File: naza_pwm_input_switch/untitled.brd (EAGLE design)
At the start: 86.3 x 50.5 mm, 30 parts, among them T1 BC847, T10 BC847, T11 BC847, T12 BC847, T2 BC847, T3 BC847, T4 BC847, T5 BC847, T6 BC847, T7 BC847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

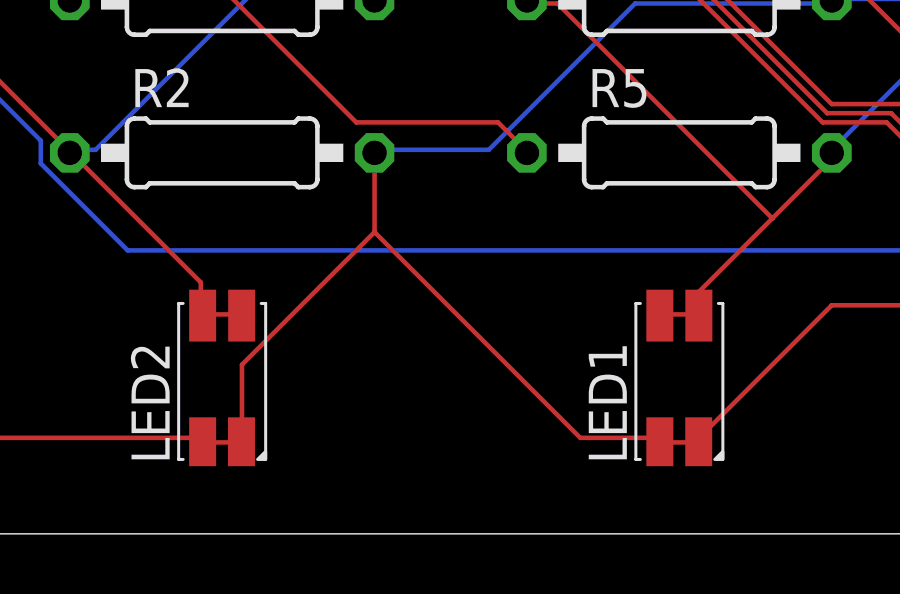
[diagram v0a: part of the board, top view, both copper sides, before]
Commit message: adjusting PCB-pwm-input-switch led voltage
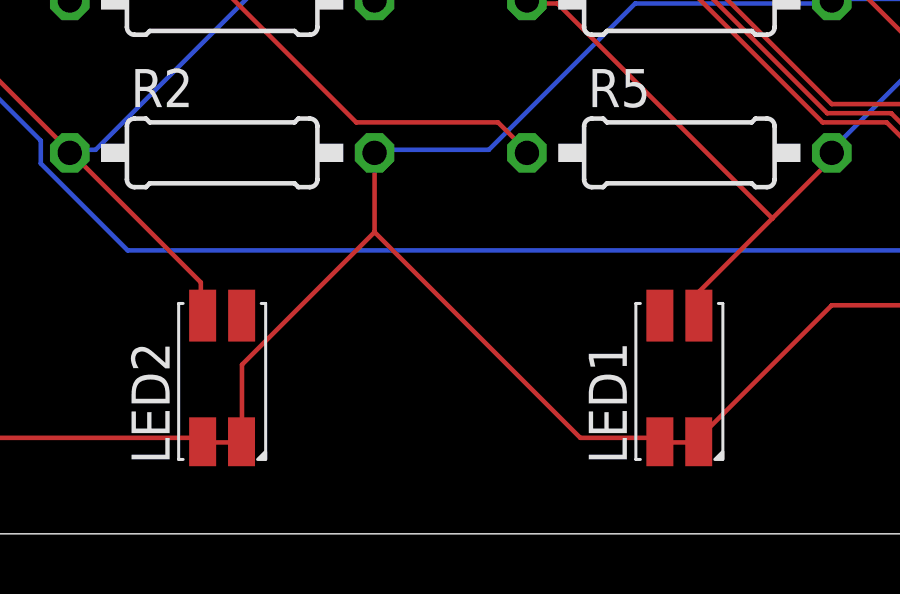
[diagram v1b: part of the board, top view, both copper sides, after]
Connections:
- net N$15: now also LED2.2, LED2.4
- net N$22: now also LED1.2, LED1.4
- net N$23: no longer LED1.2, LED1.4
- net N$24: no longer LED2.2, LED2.4
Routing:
- net N$24: track 147.0 -> 145.6 mm
- net N$23: track 96.6 -> 95.3 mm
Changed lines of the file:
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@@
 <contactref element="R1" pad="2"/>
 <contactref element="R2" pad="1"/>
-<contactref element="LED2" pad="2"/>
-<contactref element="LED2" pad="4"/>
-<wire x1="33.528" y1="7.3152" x2="32.4612" y2="7.3152" width="0.1524" layer="1"/>
-<wire x1="32.4612" y1="7.3152" x2="32.37" y2="7.275" width="0.1524" layer="1"/>
-<wire x1="33.528" y1="7.3152" x2="33.67" y2="7.275" width="0.1524" layer="1"/>
 <wire x1="28.194" y1="28.8036" x2="28.194" y2="44.5008" width="0.1524" layer="1"/>
 <wire x1="21.9456" y1="22.5552" x2="28.194" y2="28.8036" width="0.1524" layer="1"/>
@@
 <wire x1="32.3088" y1="8.382" x2="32.3088" y2="7.3152" width="0.1524" layer="1"/>
 <wire x1="28.0416" y1="12.6492" x2="32.3088" y2="8.382" width="0.1524" layer="1"/>
-<wire x1="32.3088" y1="7.3152" x2="32.37" y2="7.275" width="0.1524" layer="1"/>
 <wire x1="28.0416" y1="12.6492" x2="27.94" y2="12.7" width="0.1524" layer="1"/>
 <wire x1="43.5864" y1="47.5488" x2="43.5864" y2="44.6532" width="0.1524" layer="1"/>
@@
 <wire x1="21.6408" y1="19.05" x2="21.59" y2="19.05" width="0.1524" layer="1"/>
 <wire x1="27.8892" y1="17.8308" x2="27.94" y2="17.78" width="0.1524" layer="1"/>
+<contactref element="LED2" pad="2"/>
+<contactref element="LED2" pad="4"/>
+<wire x1="32.37" y1="7.275" x2="27.94" y2="17.78" width="0" layer="19" extent="1-1"/>
+<wire x1="33.67" y1="7.275" x2="32.37" y2="7.275" width="0" layer="19" extent="1-1"/>
 </signal>
 <signal name="N$22">
@@
 <wire x1="21.6408" y1="21.4884" x2="21.59" y2="21.59" width="0.1524" layer="1"/>
 <wire x1="43.1292" y1="12.8016" x2="43.18" y2="12.7" width="0.1524" layer="1"/>
+<contactref element="LED1" pad="2"/>
+<contactref element="LED1" pad="4"/>
+<wire x1="47.61" y1="7.275" x2="48.91" y2="7.275" width="0" layer="19" extent="1-1"/>
+<wire x1="43.18" y1="12.7" x2="47.61" y2="7.275" width="0" layer="19" extent="1-1"/>
 </signal>
 <signal name="N$23">
@@
 <contactref element="T10" pad="1"/>
 <contactref element="T11" pad="1"/>
-<contactref element="LED1" pad="2"/>
-<contactref element="LED1" pad="4"/>
 <wire x1="28.3464" y1="27.2796" x2="28.3464" y2="24.384" width="0.1524" layer="1"/>
 <wire x1="28.8036" y1="27.7368" x2="28.3464" y2="27.2796" width="0.1524" layer="1"/>
@@
 <wire x1="51.2064" y1="24.384" x2="51.12" y2="24.3" width="0.1524" layer="1"/>
 <wire x1="58.674" y1="24.384" x2="58.74" y2="24.3" width="0.1524" layer="1"/>
-<wire x1="48.768" y1="7.3152" x2="47.7012" y2="7.3152" width="0.1524" layer="1"/>
-<wire x1="47.7012" y1="7.3152" x2="47.61" y2="7.275" width="0.1524" layer="1"/>
-<wire x1="48.768" y1="7.3152" x2="48.91" y2="7.275" width="0.1524" layer="1"/>
 <wire x1="66.294" y1="22.2504" x2="66.294" y2="24.2316" width="0.1524" layer="1"/>
 <wire x1="62.1792" y1="18.1356" x2="62.9412" y2="18.8976" width="0.1524" layer="16"/>
@@
 <wire x1="51.3588" y1="10.5156" x2="48.9204" y2="8.0772" width="0.1524" layer="1"/>
 <wire x1="53.34" y1="12.6492" x2="53.34" y2="12.4968" width="0.1524" layer="1"/>
-<wire x1="48.9204" y1="7.3152" x2="48.91" y2="7.275" width="0.1524" layer="1"/>
 <wire x1="53.34" y1="12.6492" x2="53.34" y2="12.7" width="0.1524" layer="1"/>
 <wire x1="44.196" y1="17.6784" x2="43.2816" y2="17.6784" width="0.1524" layer="1"/>
